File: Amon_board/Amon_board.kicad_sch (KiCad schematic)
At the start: 39 parts, among them J1 USB2.0_C_Rev, J2 Conn_2x5 pin, SW1 SW_DPDT, SW2 SW_SPST, U1 USBLC6-2P6, U2 STM32F405RGT6-LQFP64, U3 W25Q128JVS, Y1 25MHz

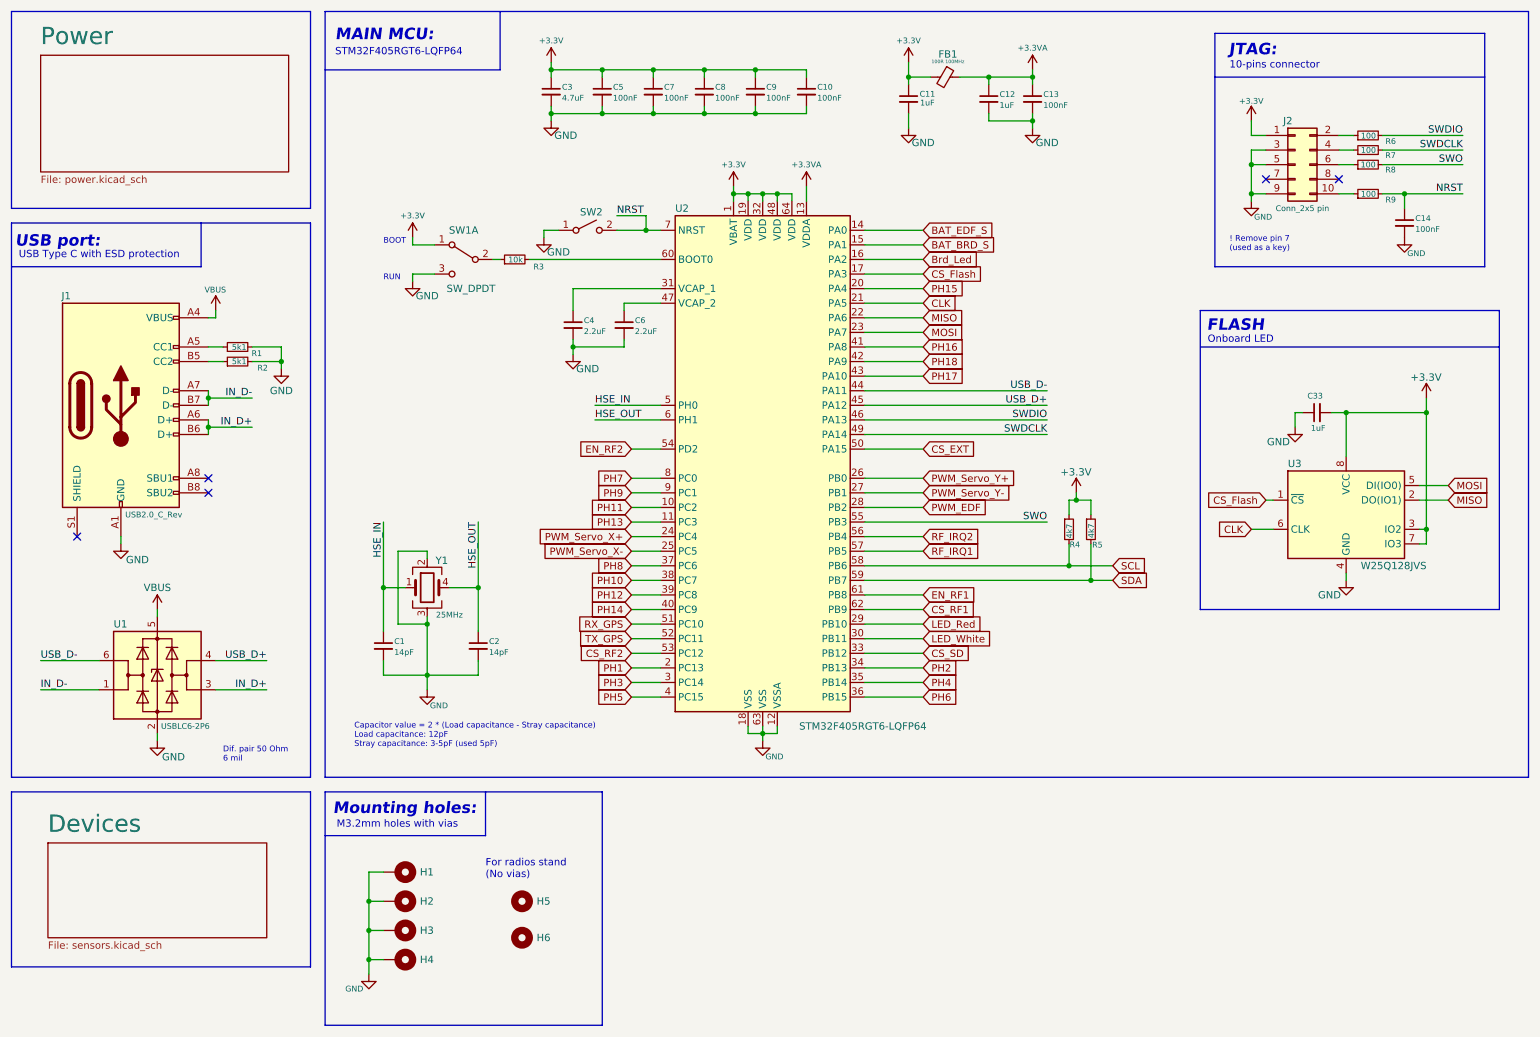
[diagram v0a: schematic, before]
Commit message: PCB update, stl update (pcb holder)
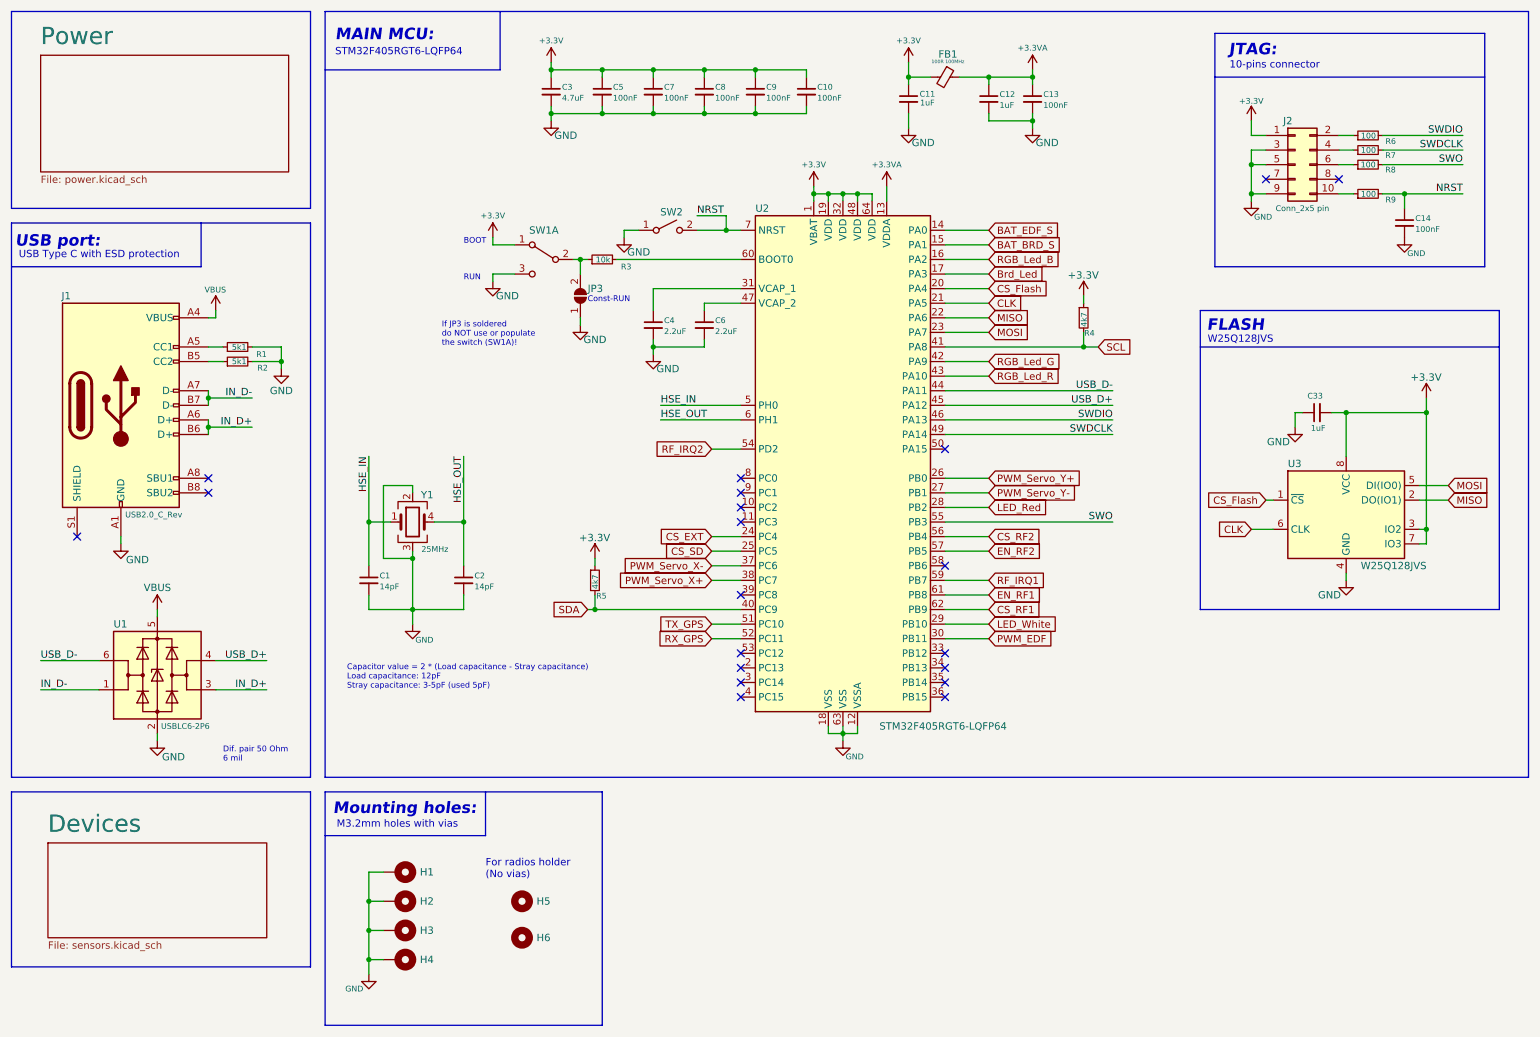
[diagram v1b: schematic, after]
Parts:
- added JP3: SolderJumper_2_Open, Jumper:SolderJumper-2_P1.3mm_Open_TrianglePad1.0x1.5mm, symbol Jumper:SolderJumper_2_Open
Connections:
- net PH10 is gone; now on net PWM_Servo_X+: U2.38 (PC7)
- net PH14 is gone; now on net SDA: U2.40 (PC9)
- net PH15 is gone; now on net CS_Flash: U2.20 (PA4)
- net PH16 is gone; now on net SCL: U2.41 (PA8)
- net PH8 is gone; now on net PWM_Servo_X-: U2.37 (PC6)
- net Brd_Led: now also U2.17 (PA3); no longer U2.16 (PA2)
- net CS_EXT: now also U2.24 (PC4); no longer U2.50 (PA15)
- net CS_Flash: no longer U2.17 (PA3)
- net CS_RF2: now also U2.56 (PB4); no longer U2.53 (PC12)
- net CS_SD: now also U2.25 (PC5); no longer U2.33 (PB12)
- net EN_RF2: now also U2.57 (PB5); no longer U2.54 (PD2)
- net GND: now also JP3.1 (A)
- net LED_Red: now also U2.28 (PB2); no longer U2.29 (PB10)
- net LED_White: now also U2.29 (PB10); no longer U2.30 (PB11)
- net PWM_EDF: now also U2.30 (PB11); no longer U2.28 (PB2)
- net PWM_Servo_X+: no longer U2.24 (PC4)
- net PWM_Servo_X-: no longer U2.25 (PC5)
- net RF_IRQ1: now also U2.59 (PB7); no longer U2.57 (PB5)
- net RF_IRQ2: now also U2.54 (PD2); no longer U2.56 (PB4)
- net RX_GPS: now also U2.52 (PC11); no longer U2.51 (PC10)
- net SCL: no longer U2.58 (PB6)
- net SDA: no longer U2.59 (PB7)
- net TX_GPS: now also U2.51 (PC10); no longer U2.52 (PC11)
- net at R3.1, SW1.2 (B): now also JP3.2 (B)
- net PH1: no longer names the net of U2.2 (PC13)
- net PH11: no longer names the net of U2.10 (PC2)
- net PH12: no longer names the net of U2.39 (PC8)
- net PH13: no longer names the net of U2.11 (PC3)
- net PH17 renamed RGB_Led_R
- net PH18 renamed RGB_Led_G
- net PH2: no longer names the net of U2.34 (PB13)
- net PH3: no longer names the net of U2.3 (PC14)
- net PH4: no longer names the net of U2.35 (PB14)
- net PH5: no longer names the net of U2.4 (PC15)
- net PH6: no longer names the net of U2.36 (PB15)
- net PH7: no longer names the net of U2.8 (PC0)
- net PH9: no longer names the net of U2.9 (PC1)
- new net RGB_Led_B: U2.16 (PA2)
- no-connect marks 5 -> 20
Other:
- note added: "Const-RUN"
- note added: "For radios holder (No vias)"
- note added: "If JP3 is soldered do NOT use or populate the switch (SW1A)!"
- note added: "W25Q128JVS"
- note removed: "! Remove pin 7 (used as a key)"
- note removed: "For radios stand (No vias)"
- note removed: "Onboard LED"
- moved on the sheet: C1, C2, C4, C6, R3, R4, SW1A, SW2, U2, Y1

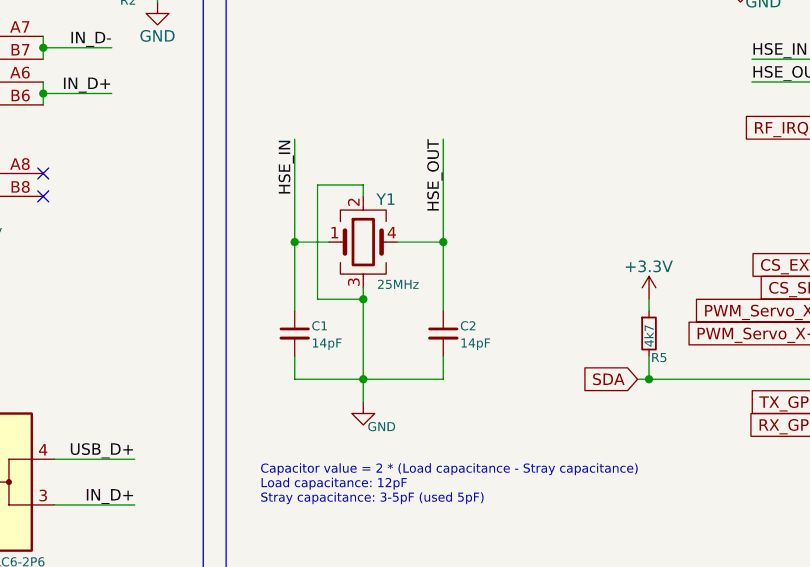
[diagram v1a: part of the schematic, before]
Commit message: PCB repair: crystal footprint, radio connector fliped, text
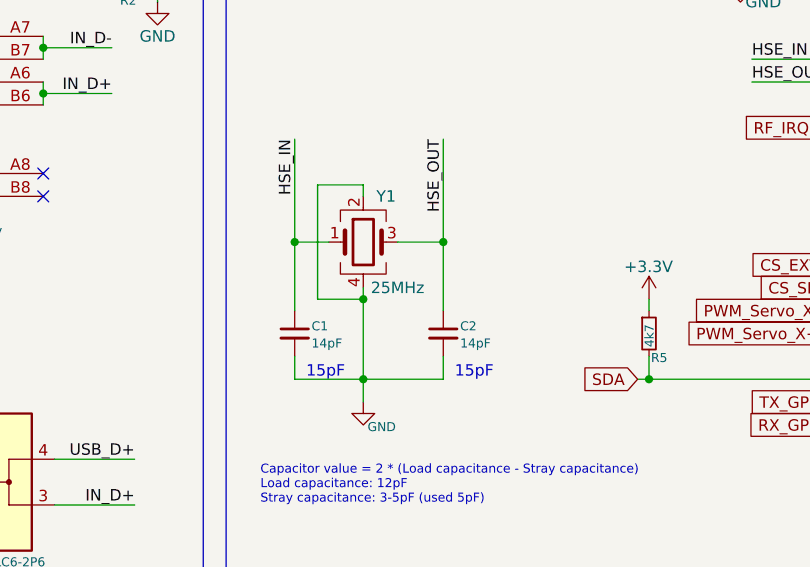
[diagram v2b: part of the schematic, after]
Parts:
- removed Y1: 25MHz, Crystal:Crystal_SMD_3225-4Pin_3.2x2.5mm, symbol Device:Crystal_GND23
- added Y1: 25MHz, Crystal:Crystal_SMD_3225-4Pin_3.2x2.5mm, symbol Device:Crystal_GND24
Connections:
- net GND: now also Y1.2, Y1.4
- net HSE_IN: now also Y1.1
- net HSE_OUT: now also Y1.3
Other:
- note added: "15pF"
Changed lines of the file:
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@@
     (stroke (width 0) (type default) (color 0 0 0 0))
+  )
+  (text "15pF" (at 78.74 118.11 0)
+    (effects (font (size 1.27 1.27)) (justify left bottom))
   )
   (text "W25Q128JVS" (at 223.5239 71.8954 0)
@@
     (at 90.17 72.39 0)
     (effects (font (size 1 1)) (justify left bottom))
+  )
+  (text "15pF" (at 95.25 118.11 0)
+    (effects (font (size 1.27 1.27)) (justify left bottom))
   )
   (text "Capacitor value = 2 * (Load capacitance - Stray capacitance)\nLoad capacitance: 12pF\nStray capacitance: 3-5pF (used 5pF)\n"
@@
     (pin "2")
   )
+  (symbol (lib_id "Device:Crystal_GND24") (at 85.09 102.87 0) (unit 1)
+    (in_bom yes) (on_board yes)
+    (property "Reference" "Y1" (id 0) (at 87.63 97.79 0))
+    (property "Value" "25MHz" (id 1) (at 88.9 107.95 0))
+    (property "Footprint" "Crystal:Crystal_SMD_3225-4Pin_3.2x2.5mm" (id 2) (at 85.09 102.87 0)
+      (effects (font (size 1.27 1.27)) hide)
+    )
+    (property "Datasheet" "~" (id 3) (at 85.09 102.87 0)
+      (effects (font (size 1.27 1.27)) hide)
+    )
+    (pin "1")
+    (pin "2")
+    (pin "3")
+    (pin "4")
+  )
   (symbol (lib_id "Device:C_Small") (at 93.98 113.03 0) (unit 1)
     (in_bom yes) (on_board yes)
@@
     )
     (pin "1")
-  )
-  (symbol (lib_id "Device:Crystal_GND23") (at 85.09 102.87 0) (unit 1)
-    (in_bom yes) (on_board yes)
-    (property "Reference" "Y1" (id 0) (at 87.6299 98.1497 0))
-    (property "Value" "25MHz" (id 1) (at 88.9622 107.6045 0)
-      (effects (font (size 1 1)))
-    )
-    (property "Footprint" "Crystal:Crystal_SMD_3225-4Pin_3.2x2.5mm" (id 2) (at 85.09 102.87 0)
-      (effects (font (size 1.27 1.27)) hide)
-    )
-    (property "Datasheet" "~" (id 3) (at 85.09 102.87 0)
-      (effects (font (size 1.27 1.27)) hide)
-    )
-    (pin "1")
-    (pin "2")
-    (pin "3")
-    (pin "4")
   )
   (symbol (lib_id "power:GND") (at 193.04 34.29 0) (unit 1)
@@
       (reference "U7") (unit 1) (value "BME280") (footprint "Package_LGA:Bosch_LGA-8_2x2.5mm_P0.65mm_ClockwisePinNumbering")
     )
-    (path "/9e2b8aaa-8eac-4e0c-9bf7-66548d55f57b"
+    (path "/7874607d-341d-4bfa-86e4-db94d15f43c6"
       (reference "Y1") (unit 1) (value "25MHz") (footprint "Crystal:Crystal_SMD_3225-4Pin_3.2x2.5mm")
     )

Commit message: changed directories
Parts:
- added C37: 100nF, Capacitor_SMD:C_0603_1608Metric, symbol Device:C_Small
- added R36, R37: 22, Resistor_SMD:R_0603_1608Metric, symbol Device:R_Small
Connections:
- net GND: now also C37.2
- net IN_D+: now also U1.1 (I/O1), R37.2; no longer J1.A6 (D+), J1.B6 (D+), U1.3 (I/O2)
- net IN_D-: now also U1.3 (I/O2), R36.2; no longer J1.A7 (D-), J1.B7 (D-), U1.1 (I/O1)
- net RGB_Led_B: now also U2.42 (PA9); no longer U2.16 (PA2)
- net RGB_Led_G: now also U2.43 (PA10); no longer U2.42 (PA9)
- net RGB_Led_R: now also U2.16 (PA2); no longer U2.43 (PA10)
- net USB_D+: now also U1.6 (I/O1); no longer U1.4 (I/O2)
- net USB_D-: now also U1.4 (I/O2); no longer U1.6 (I/O1)
- net VBUS: now also C37.1
- new net: J1.A7 (D-), J1.B7 (D-), R36.1
- new net: J1.A6 (D+), J1.B6 (D+), R37.1
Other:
- moved on the sheet: J1, R1, R2, U1
